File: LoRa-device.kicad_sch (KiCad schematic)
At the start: 113 parts, among them J1 Connector, USB-TYPE-C-16P, J2 Conn_01x02_Pin, J3 Conn_Coaxial, J4 Conn_01x14_Pin, J6 Conn_01x04_Pin, J7 Screw_Terminal_01x08, J8 U.FL, Q1 AO3401A, Q2 S8050, SW1 SW_Nidec_CAS-120A1, U1 ESP32-S3, U11 L76KB-A58, U2 W25Q128JVS, U3 TP4055, U4 ATECC608A-SSHDA, U5 Ai-Thinker-Ra-01, U6 USBLC6-2P6, U8 TPS22917LDBV, U9 AP63203WU, Y1 32.768 kHz, Y2 40MHz(10ppm)

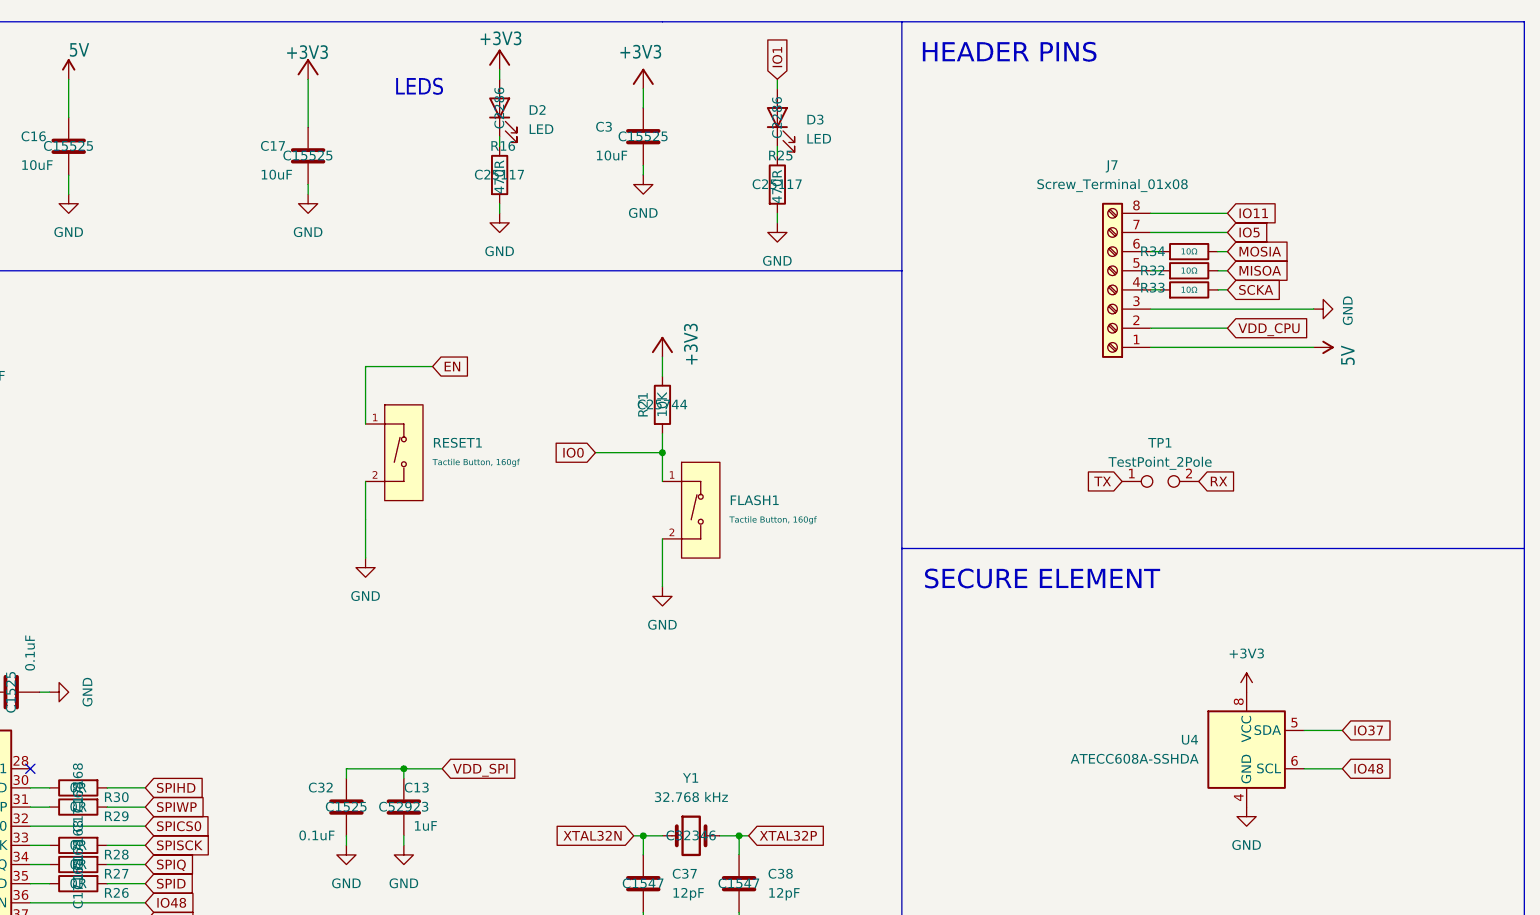
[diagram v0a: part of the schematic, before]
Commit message: 3d model, case space for battery.
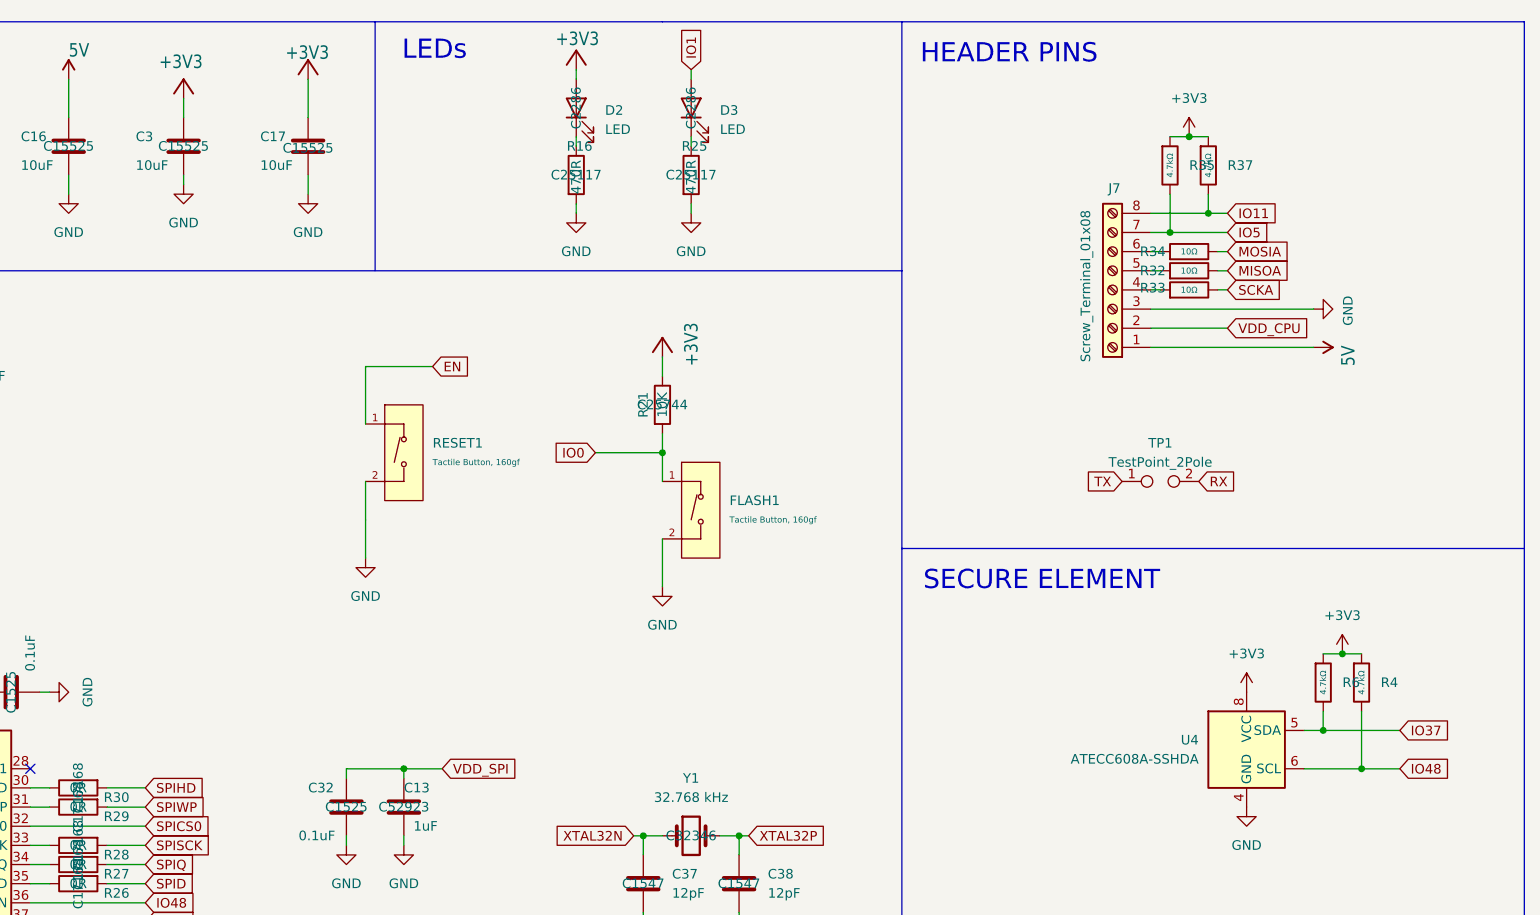
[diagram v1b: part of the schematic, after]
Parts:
- added R35, R37, R4, R6: 4.7kΩ, PCM_JLCPCB:R_0402, symbol PCM_JLCPCB-Resistors:0402,4.7kΩ
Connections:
- net +3V3: now also R35.1, R37.1, R4.1, R6.1
- net IO11: now also R37.2
- net IO37: now also R6.2
- net IO48: now also R4.2
- net IO5: now also R35.2
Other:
- note added: "LEDs"
- note removed: "LEDS"
- moved on the sheet: C17, C3, D2, D3, R16, R25

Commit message: External header protection, clean routing
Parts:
- added D6, D7: PMEG2010AEH, Diode_SMD:D_SOD-123F, symbol Diode:PMEG2010AEH
- added F1, F2: Polyfuse, Fuse:Fuse_0603_1608Metric, symbol Device:Polyfuse
- added R38, R39: 10Ω, Resistor_SMD:R_0402_1005Metric, symbol PCM_JLCPCB-Resistors:0402,10Ω
- added R40: 100kΩ, PCM_JLCPCB:R_0402, symbol PCM_JLCPCB-Resistors:0402,100kΩ
- added R41: 47Ω, PCM_JLCPCB:R_0402, symbol PCM_JLCPCB-Resistors:0402,47Ω
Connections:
- net +3V3: now also F2.2, R40.1; no longer J7.2 (Pin_2)
- net 5V: now also F1.2; no longer J7.1 (Pin_1)
- net IO18: now also J4.11 (Pin_11), R11.2; no longer U5.4 (~{RESET})
- net IO33: now also R39.2; no longer R10.2, U5.15 (~{NSS})
- net IO34: now also R10.2, U5.15 (~{NSS}); no longer J4.5 (Pin_5)
- net IO36: now also U5.6 (DIO1); no longer J4.11 (Pin_11), R11.2
- net IO37: now also U5.4 (~{RESET}); no longer R6.2, U4.5 (SDA)
- net IO47: now also R6.2, U4.5 (SDA); no longer U5.6 (DIO1)
- net IO5: now also J4.5 (Pin_5); no longer J7.7 (Pin_7), R35.2
- net IO6: now also J4.14 (Pin_14); no longer U11.4 (1PPS)
- net IO7: now also R38.2; no longer U11.9 (RESET_N)
- net MISOA: now also R40.2, R41.2; no longer J6.3 (Pin_3)
- net IO11: no longer names the net of J7.8 (Pin_8), R37.2
- net IO11: now also R38.1; no longer U1.16 (GPIO11)
- net IO4/BAT renamed IO11/BAT
- net IO11/BAT: now also U1.16 (GPIO11); no longer U1.9 (GPIO4)
- new net: D6.1 (K), J7.2 (Pin_2)
- new net: D6.2 (A), F2.1
- new net: D7.1 (K), J7.1 (Pin_1)
- new net: J7.7 (Pin_7), R35.2, R39.1
- new net: J6.3 (Pin_3), R41.1
- new net: D7.2 (A), F1.1
- new net IO4: U1.9 (GPIO4), U11.9 (RESET_N)
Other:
- moved on the sheet: J6, TP1

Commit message: L76K V_BCKP added
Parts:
- removed D6, D7: PMEG2010AEH, Diode_SMD:D_SOD-123F, symbol Diode:PMEG2010AEH
- removed F1, F2: Polyfuse, Fuse:Fuse_0603_1608Metric, symbol Device:Polyfuse
- removed R32, R33, R34, R38, R39: 10Ω, Resistor_SMD:R_0402_1005Metric, symbol PCM_JLCPCB-Resistors:0402,10Ω
- added C30, C34, C41: 1uF, PCM_JLCPCB:C_0402, symbol PCM_JLCPCB-Capacitors:0402,1uF
- added R42, R43, R44, R45, R46: 100Ω, PCM_JLCPCB:R_0402, symbol PCM_JLCPCB-Resistors:0402,100Ω
- added U7: STLQ015M33R, Lora-device:SOT-23-5_L3.0-W1.7-P0.95-LS2.8-BR, symbol Lora-device:STLQ015M33R
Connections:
- net +3V3: now also J7.1 (Pin_1), J7.2 (Pin_2), C30.1; no longer U11.6 (V_BCKP)
- net GND: now also C30.2, C34.2, C41.2, U7.2 (GND)
- net IO33: now also R44.2
- net IO7: now also R43.2
- net MISOA: now also R45.2
- net MOSIA: now also R42.2
- net SCKA: now also R46.2
- net VBAT: now also C41.1, U7.1 (IN), U7.3 (EN)
- net at J7.4 (Pin_4): now also R46.1
- net at J7.5 (Pin_5): now also R45.1
- net at J7.6 (Pin_6): now also R42.1
- net at J7.7 (Pin_7), R35.2: now also R44.1
- net at J7.8 (Pin_8), R37.2: now also R43.1
- new net: C34.1, U11.6 (V_BCKP), U7.5 (OUT)
- no-connect marks 17 -> 18
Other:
- note added: "SWITCH"
